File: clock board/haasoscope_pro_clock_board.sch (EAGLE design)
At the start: 8 parts, among them IC1 LMX2582RHAT, J3 2X4P-2.54

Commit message: initial adf4350
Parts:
- removed IC1: LMX2582RHAT, LMX2582RHAT:LMX2582RHAT
- added C28, C29, C37, C57, C58: 1U, capacitor:C0603_90
- added C30: 10N, capacitor:C0402_55
- added C31: 22U, capacitor:CPOL7343-43
- added C38, C40, C42, C45, C46, C48, C50, C52: 10P, capacitor:C0402_55
- added C39, C41, C43, C44, C47, C49, C51, C53, C56: 100N, capacitor:C0402_55
- added C54, C55: 120P, capacitor:C0402_55
- added C59, C60: 100P, capacitor:C0402_55
- added C61: 3N3, capacitor:C0603_90
- added C62: 47N, capacitor:C0603_90
- added C63: 1N5, capacitor:C0603_90
- added FB2: FB0603, inductor:FB0603
- added R10, R11, R13, R9: 10K, resistor:R0603_55
- added R14: 316, resistor:R0603_55
- added R18: 681, resistor:R0603_55
- added R22, R7: 0, resistor:R0603_55
- added R23: DNI, resistor:R0603_55
- added R24, R25: 49R9, resistor:R0402_40
- added R8: 5K11, resistor:R0603_55
- added U4: ADF4350BCPZ, analog_devices:ADF4350BCPZ
- added U5, U6: ADP150AUJZ-3.3, analog_devices:ADP150AUJZ-3.3
- added Y2: XO_E5X3, oscillator:XO_E5X3
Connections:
- new net 3V3: C29.2, C38.2, C39.2, C40.1, C41.1, C42.2, C43.2, C44.2, C45.2, C46.2, C47.2, FB2.2, R9.2, U4G$1.AVDD, U4G$1.DVDD, U4G$1.PDBRF, U4G$1.SDVDD, U4G$1.VP, U4G$1.VVCO@16, U4G$1.VVCO@17, U5.VOUT
- new net ADFCE: R9.1, U4G$1.CE
- new net ADFCLK: R10.2, U4G$1.CLK
- new net ADFDATA: R11.2, U4G$1.DATA
- new net ADFLE: R13.2, U4G$1.LE
- new net LD: U4G$1.LD
- new net MUXOUT: U4G$1.MUXOUT
- new net N$13: R7.1, Y2.OUT
- new net N$18: C48.2, C49.2, U4G$1.TEMP
- new net N$19: C50.2, C51.2, U4G$1.VCOM
- new net N$31: R8.1, U4G$1.RSET
- new net N$4: C30.2, C37.2, FB2.1, Y2.EN, Y2.VDD
- new net N$40: C60.2
- new net N$41: C59.2
- new net N$42: C61.2, C62.1, R18.2, U4G$1.CPOUT
- new net N$44: C62.2, R14.1
- new net N$45: R14.2, R22.2, R23.1
- new net N$46: R23.2, U4G$1.SW
- new net REFOUTA_N: C60.1, R25.1, U4G$1.RFOUTA-
- new net REFOUTA_P: C59.1, R24.1, U4G$1.RFOUTA+
- new net REF_CLK: R7.2, U4G$1.REFIN
- new net VIN: C28.2, C31.1, C57.2, U5.EN, U5.VIN, U6.EN, U6.VIN
- new net VOUT: C54.2, C55.2, C56.2, C58.2, R24.2, R25.2, U6.VOUT
- new net VREF: C52.1, C53.1, U4G$1.VREF
- new net VTUNE: C63.2, R18.1, U4G$1.VTUNE
- net GND: now also C28.1, C29.1, C30.1, C31.2, C37.1, C38.1, C39.1, C40.2, C41.2, C42.1, C43.1, C44.1, C45.1, C46.1, C47.1, C48.1, C49.1, C50.1, C51.1, C52.2, C53.2, C54.1, C55.1, C56.1, C57.1, C58.1, C61.1, C63.1, R10.1, R11.1, R13.1, R22.1, R8.2, U4G$1.AGND, U4G$1.AGNDVCO@11, U4G$1.AGNDVCO@18, U4G$1.AGNDVCO@21, U4G$1.CPGND, U4G$1.DGND, U4G$1.SDGND, U5.GND, U6.GND, Y2.GND
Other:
- note added: "CP: 2.50mA"
- note added: "Loop BW: 30.0kHz"
- note added: "Phase Margin: 45.0deg"
- note added: "R2: 681"
- note added: "Rset: 5.10k"

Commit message: v1.0
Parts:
- removed AOUT+, AOUT-: BU-SMB-V, con-coax:BU-SMB-V
- removed C28, C29, C37, C57, C58: 1U, capacitor:C0603_90
- removed C30: 10N, capacitor:C0402_55
- removed C31: 22U, capacitor:CPOL7343-43
- removed C38, C40, C42, C45, C46, C48, C50, C52: 10P, capacitor:C0402_55
- removed C39, C41, C43, C44, C47, C49, C51, C53, C56: 100N, capacitor:C0402_55
- removed C54, C55: 120P, capacitor:C0402_55
- removed C59, C60: 100P, capacitor:C0402_55
- removed C61: 3N3, capacitor:C0603_90
- removed C62: 47N, capacitor:C0603_90
- removed C63: 1N5, capacitor:C0603_90
- removed FB2: FB0603, inductor:FB0603
- removed J3: 2X4P-2.54, Seeed-Connector:DIP-BLACK-FEMALE-HEADER(2X4P-2.54)
- removed R13: 10K, resistor:R0603_55
- removed R14: 316, resistor:R0603_55
- removed R18: 681, resistor:R0603_55
- removed R22: 0, resistor:R0603_55
- removed R23: DNI, resistor:R0603_55
- removed R24, R25: 49R9, resistor:R0402_40
- removed U5, U6: ADP150AUJZ-3.3, analog_devices:ADP150AUJZ-3.3
- removed Y2: XO_E5X3, oscillator:XO_E5X3
- added C10, C11: 0.1nF, MF_Passives:CAPACITOR_NP_0402
- added C12, C13: 1nF, MF_Passives:CAPACITOR_NP_0402
- added C14: 2.7nF, MF_Passives:CAPACITOR_NP_0402
- added C15: 47nF, MF_Passives:CAPACITOR_NP_0402
- added C16: 680pF, MF_Passives:CAPACITOR_NP_0402
- added C3, C4, C5, C6, C7, C8, C9: 0.1uF, MF_Passives:CAPACITOR_NP_0402
- added J4: 8pin, SparkFun-Connectors:CONN_08"
- added R1: 47, MF_Passives:RESISTOR_0402
- added R4, R5, R6: 10k, MF_Passives:RESISTOR_0402
- added REFRFIN, RFAOUT+, RFAOUT-: (no value), adafruit:SMACONNECTOR_EDGE
- R10: value 10K -> 1k; device resistor:R0603_55 -> MF_Passives:RESISTOR_0402
- R11: value 10K -> 360; device resistor:R0603_55 -> MF_Passives:RESISTOR_0402
- R2: value 40 -> 0
- R3: value 40 -> 47
- R7: value 0 -> 10k; device resistor:R0603_55 -> MF_Passives:RESISTOR_0402
- R8: value 5K11 -> 5.1k; device resistor:R0603_55 -> MF_Passives:RESISTOR_0402
- R9: value 10K -> 47; device resistor:R0603_55 -> MF_Passives:RESISTOR_0402
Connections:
- removed net 3V3: C29.2, C38.2, C39.2, C40.1, C41.1, C42.2, C43.2, C44.2, C45.2, C46.2, C47.2, FB2.2, R9.2, U4G$1.AVDD, U4G$1.DVDD, U4G$1.PDBRF, U4G$1.SDVDD, U4G$1.VP, U4G$1.VVCO@16, U4G$1.VVCO@17, U5.VOUT
- removed net N$13: R7.1, Y2.OUT
- removed net N$4: C30.2, C37.2, FB2.1, Y2.EN, Y2.VDD
- removed net N$40: C60.2
- removed net N$41: C59.2
- removed net N$42: C61.2, C62.1, R18.2, U4G$1.CPOUT
- removed net N$44: C62.2, R14.1
- removed net N$45: R14.2, R22.2, R23.1
- removed net N$46: R23.2, U4G$1.SW
- removed net REFOUTA_N: C60.1, R25.1, U4G$1.RFOUTA-
- removed net REFOUTA_P: C59.1, R24.1, U4G$1.RFOUTA+
- removed net VIN: C28.2, C31.1, C57.2, U5.EN, U5.VIN, U6.EN, U6.VIN
- removed net VS+: C1.P$1, J3.2
- removed net VS-: C2.P$1, J3.3
- new net +3V3: C1.P$1, C2.P$2, C6.P$2, C7.P$2, C8.P$1, J4.8, R2.P$1, R7.P$2, U4G$1.AVDD, U4G$1.DVDD, U4G$1.PDBRF, U4G$1.SDVDD, U4G$1.VP, U4G$1.VVCO@16, U4G$1.VVCO@17
- new net CPOUT: C14.P$1, R10.P$2, R11.P$1, U4G$1.CPOUT
- new net N$3: C15.P$1, R11.P$2
- new net RFOUTASMA_N: C10.P$1, RFAOUT-.ANT
- new net RFOUTASMA_P: C11.P$1, RFAOUT+.ANT
- new net RFOUTA_N: C10.P$2, R1.P$1, U4G$1.RFOUTA-
- new net RFOUTA_P: C11.P$2, R3.P$1, U4G$1.RFOUTA+
- net ADFCE: now also J4.2, R7.P$1; no longer R9.1
- net ADFCLK: now also J4.5, R6.P$2; no longer R10.2
- net ADFDATA: now also J4.4, R5.P$2; no longer R11.2
- net ADFLE: now also J4.3, R4.P$2; no longer R13.2
- net GND: now also C14.P$2, C15.P$2, C16.P$2, C2.P$1, C3.P$2, C4.P$1, C5.P$1, C6.P$1, C7.P$1, C8.P$2, C9.P$2, J4.1, R4.P$1, R5.P$1, R6.P$1, R8.P$1, R9.P$1, REFRFIN.GND1, REFRFIN.GND2, REFRFIN.GND3, REFRFIN.GND4, RFAOUT+.GND1, RFAOUT+.GND2, RFAOUT+.GND3, RFAOUT+.GND4, RFAOUT-.GND1, RFAOUT-.GND2, RFAOUT-.GND3, RFAOUT-.GND4; no longer AOUT+.2, AOUT-.2, C2.P$2, C28.1, C29.1, C30.1, C31.2, C37.1, C38.1, C39.1, C40.2, C41.2, C42.1, C43.1, C44.1, C45.1, C46.1, C47.1, C48.1, C49.1, C50.1, C51.1, C52.2, C53.2, C54.1, C55.1, C56.1, C57.1, C58.1, C61.1, C63.1, J3.1, J3.4, J3.5, J3.6, J3.7, J3.8, R10.1, R11.1, R13.1, R22.1, R8.2, U5.GND, U6.GND, Y2.GND
- net LD: now also J4.7
- net MUXOUT: now also J4.6
- net N$1: now also C12.P$2, REFRFIN.ANT; no longer AOUT+.1, R2.P$2
- net N$18: now also C5.P$2; no longer C48.2, C49.2
- net N$19: now also C4.P$2; no longer C50.2, C51.2
- net N$2: now also C12.P$1, C13.P$2, R9.P$2; no longer AOUT-.1, R3.P$2
- net N$31: now also R8.P$2; no longer R8.1
- net REF_CLK: now also C13.P$1; no longer R7.2
- net VOUT: now also C9.P$1, R1.P$2, R2.P$2, R3.P$2; no longer C54.2, C55.2, C56.2, C58.2, R24.2, R25.2, U6.VOUT
- net VREF: now also C3.P$1; no longer C52.1, C53.1
- net VTUNE: now also C16.P$1, R10.P$1; no longer C63.2, R18.1
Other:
- note removed: "CP: 2.50mA"
- note removed: "Loop BW: 30.0kHz"
- note removed: "Phase Margin: 45.0deg"
- note removed: "R2: 681"
- note removed: "Rset: 5.10k"
- moved on the sheet: C1, C2, R2, R3

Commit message: v1.0
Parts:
- REFRFIN, RFAOUT+, RFAOUT-: value (none) -> sma
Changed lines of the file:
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@@
 <part name="+3V20" library="supply1" deviceset="+3V3" device=""/>
 <part name="GND95" library="supply1" deviceset="GND" device=""/>
-<part name="RFAOUT-" library="adafruit" deviceset="SMACONNECTOR" device="_EDGE"/>
-<part name="RFAOUT+" library="adafruit" deviceset="SMACONNECTOR" device="_EDGE"/>
+<part name="RFAOUT-" library="adafruit" deviceset="SMACONNECTOR" device="_EDGE" value="sma"/>
+<part name="RFAOUT+" library="adafruit" deviceset="SMACONNECTOR" device="_EDGE" value="sma"/>
 <part name="J4" library="SparkFun-Connectors" library_urn="urn:adsk.eagle:library:513" deviceset="CONN_08" device="&quot;" package3d_urn="urn:adsk.eagle:package:38138/1" value="8pin"/>
 <part name="+3V1" library="supply1" deviceset="+3V3" device=""/>
@@
 <part name="C11" library="MF_Passives" deviceset="CAPACITOR_NP" device="_0402" value="0.1nF"/>
 <part name="GND2" library="supply1" deviceset="GND" device=""/>
-<part name="REFRFIN" library="adafruit" deviceset="SMACONNECTOR" device="_EDGE"/>
+<part name="REFRFIN" library="adafruit" deviceset="SMACONNECTOR" device="_EDGE" value="sma"/>
 <part name="C12" library="MF_Passives" deviceset="CAPACITOR_NP" device="_0402" value="1nF"/>
 <part name="R9" library="MF_Passives" deviceset="RESISTOR" device="_0402" value="47"/>

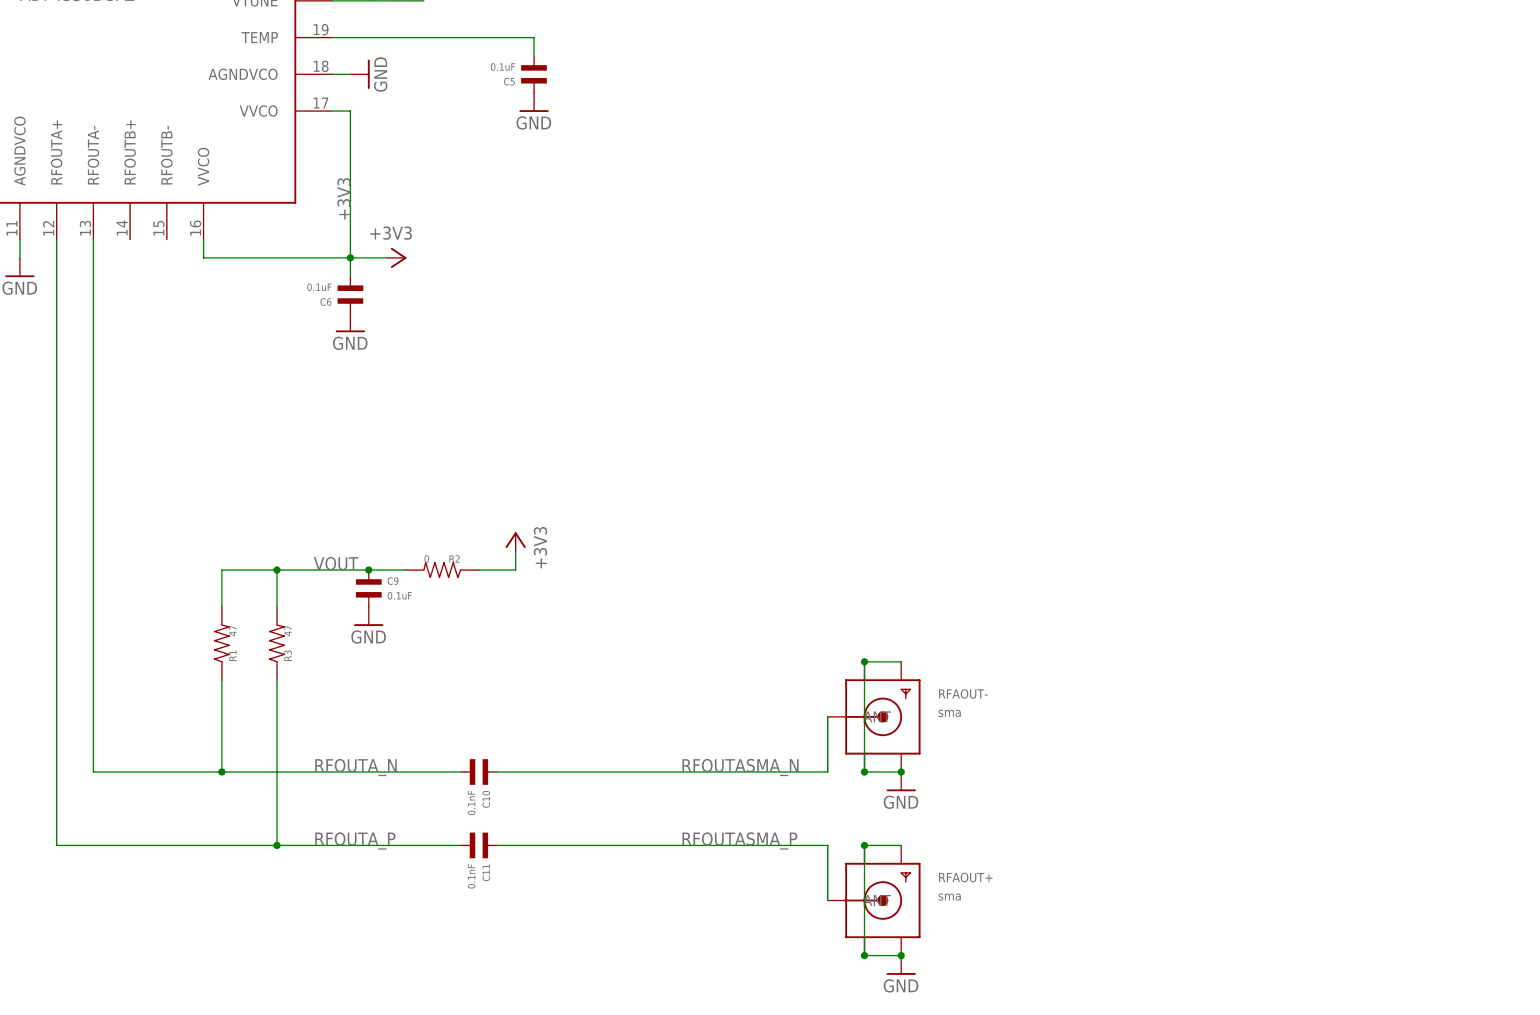
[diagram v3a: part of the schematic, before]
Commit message: add refB out, fix i/o spacing
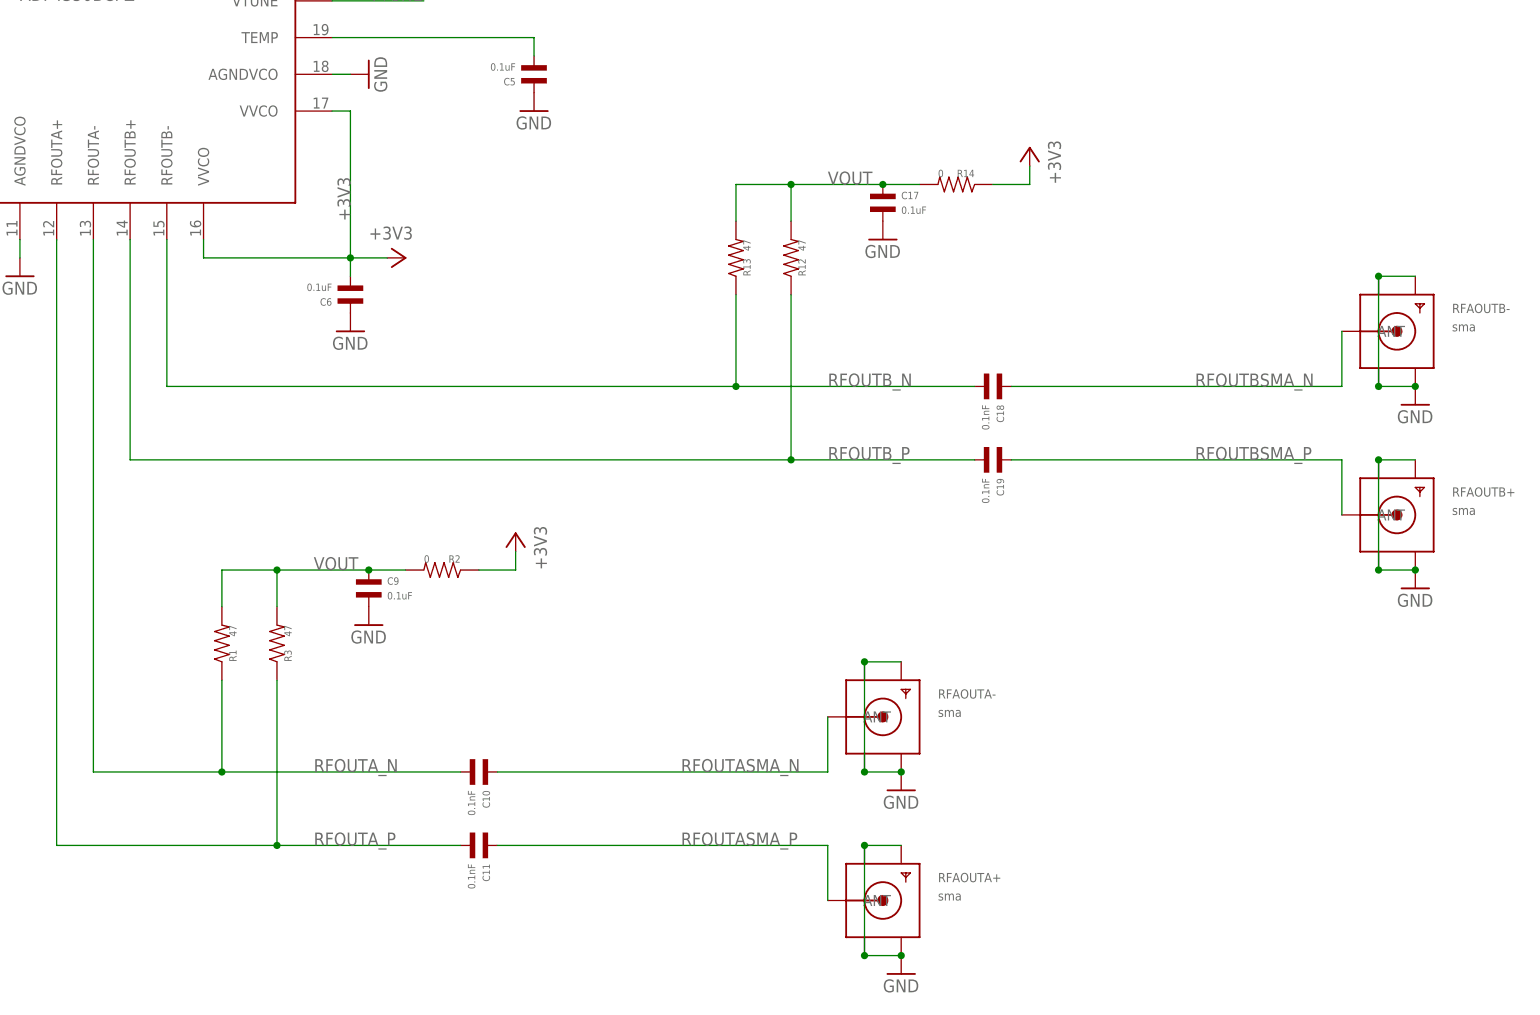
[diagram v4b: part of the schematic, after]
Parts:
- added C17: 0.1uF, MF_Passives:CAPACITOR_NP_0402
- added C18, C19: 0.1nF, MF_Passives:CAPACITOR_NP_0402
- added R12, R13: 47, MF_Passives:RESISTOR_0402
- added R14: 0, MF_Passives:RESISTOR_0402
- added RFAOUTB+, RFAOUTB-: sma, adafruit:SMACONNECTOR_EDGE
- renumbered RFAOUT+ to RFAOUTA+, RFAOUT- to RFAOUTA-
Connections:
- new net RFOUTBSMA_N: C18.P$1, RFAOUTB-.ANT
- new net RFOUTBSMA_P: C19.P$1, RFAOUTB+.ANT
- new net RFOUTB_N: C18.P$2, R13.P$1, U4G$1.RFOUTB-
- new net RFOUTB_P: C19.P$2, R12.P$1, U4G$1.RFOUTB+
- net +3V3: now also R14.P$1
- net GND: now also C17.P$2, RFAOUTB+.GND1, RFAOUTB+.GND2, RFAOUTB+.GND3, RFAOUTB+.GND4, RFAOUTB-.GND1, RFAOUTB-.GND2, RFAOUTB-.GND3, RFAOUTB-.GND4
- net VOUT: now also C17.P$1, R12.P$2, R13.P$2, R14.P$2
